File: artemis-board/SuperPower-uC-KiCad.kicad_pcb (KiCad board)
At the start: 4 copper layers, 45.1 x 45.1 mm, 97 parts, among them J1 Battery connector, J10 External NTC, J2 Thermistor, J3 USB_B_Micro, J4 Solar in, J8 regulator board, Q1 2N7002, Q10 AO3401A, Q11 2N7002, Q2 2N7002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

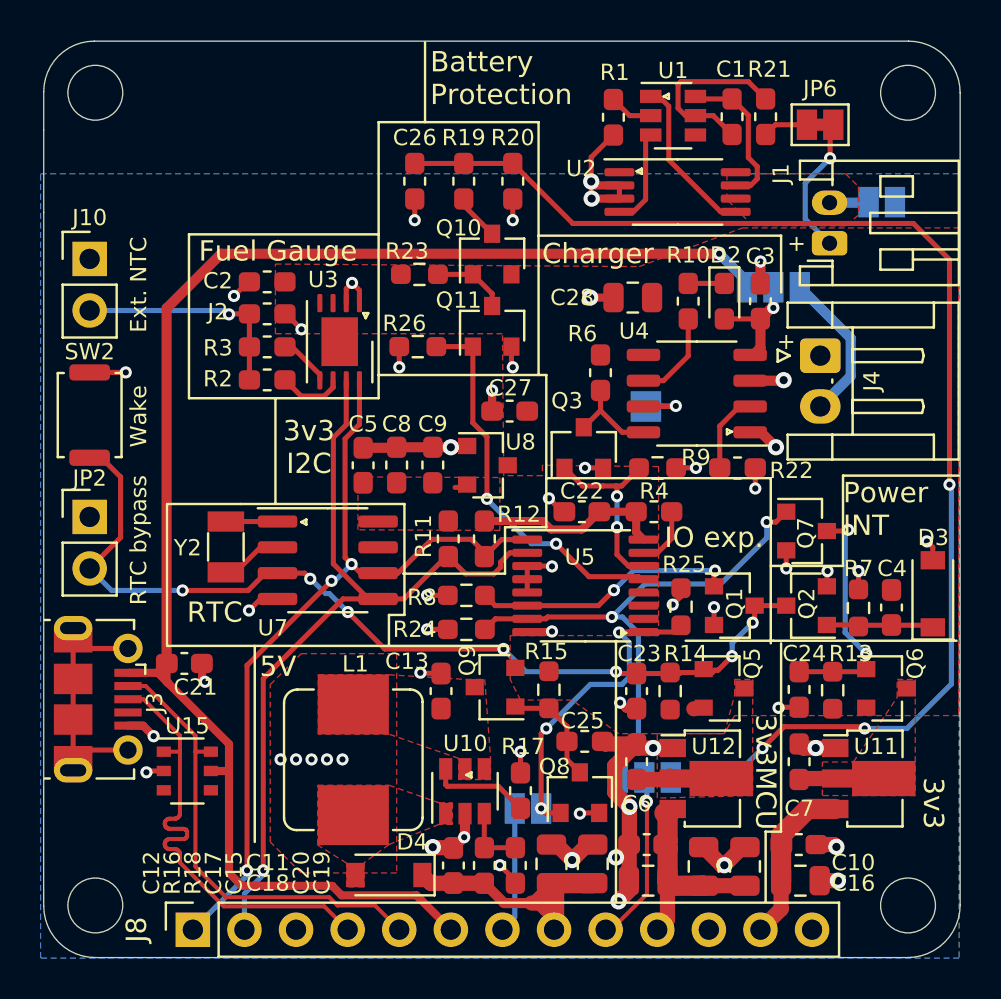
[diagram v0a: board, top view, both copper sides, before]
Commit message: added WLCSP9 footprint for LC709203
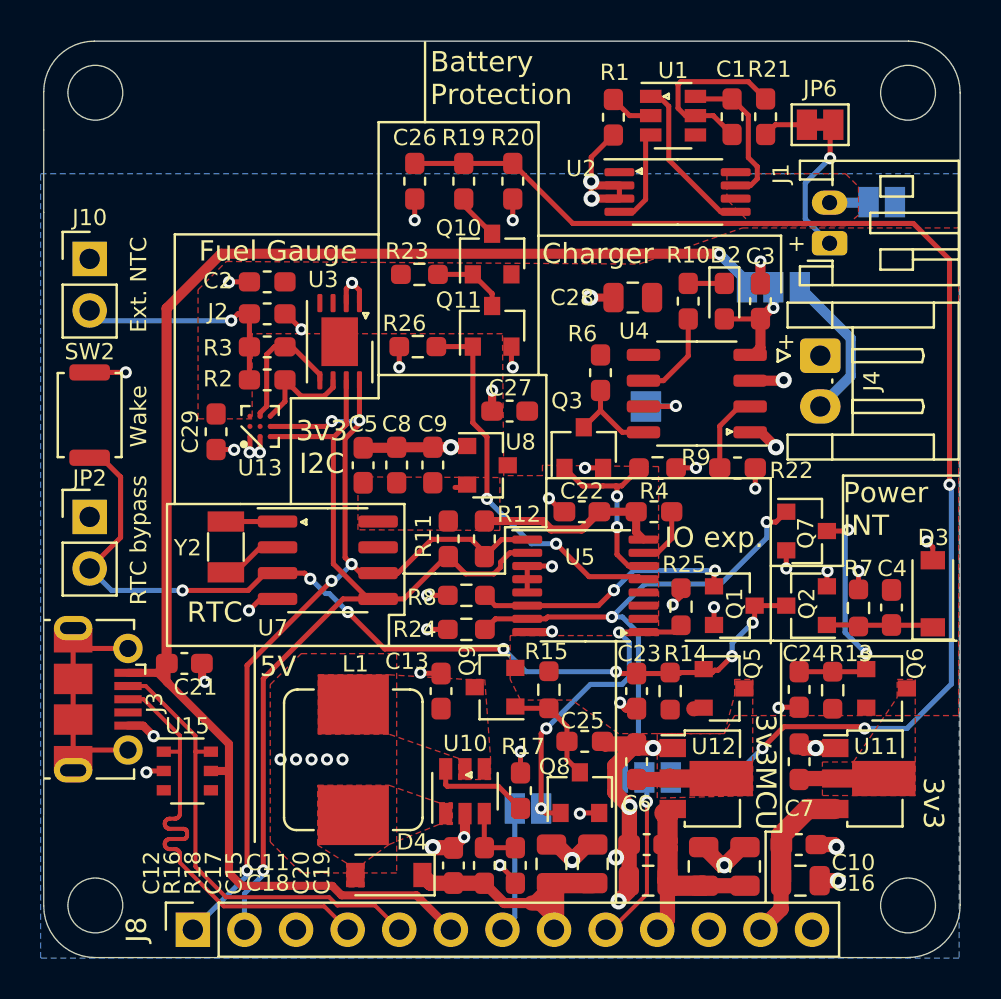
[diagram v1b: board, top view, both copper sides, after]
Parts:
- added C29: 0.1µF, Capacitor_SMD:C_0603_1608Metric_Pad1.05x0.95mm_HandSolder, F.Cu at (141.7, 97.5)
- added U13: LC709203FXE, Package_CSP:WLCSP-9_3x3_1.76x1.6mm, F.Cu at (143.9, 97.3)
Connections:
- net Net-(R2-Pad1) renamed /Charging Module/T1
- net Net-(R3-Pad1) renamed /Charging Module/T2
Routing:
- net /SCL: track 41.9 -> 46.7 mm, vias 3 -> 5
- net /Charging Module/T2: track 2.57 -> 6.80 mm
- net /SDA: track 42.6 -> 45.8 mm
- net GND: track 81.1 -> 83.6 mm, vias 56 -> 59
- net /Charging Module/T1: track 3.22 -> 5.62 mm

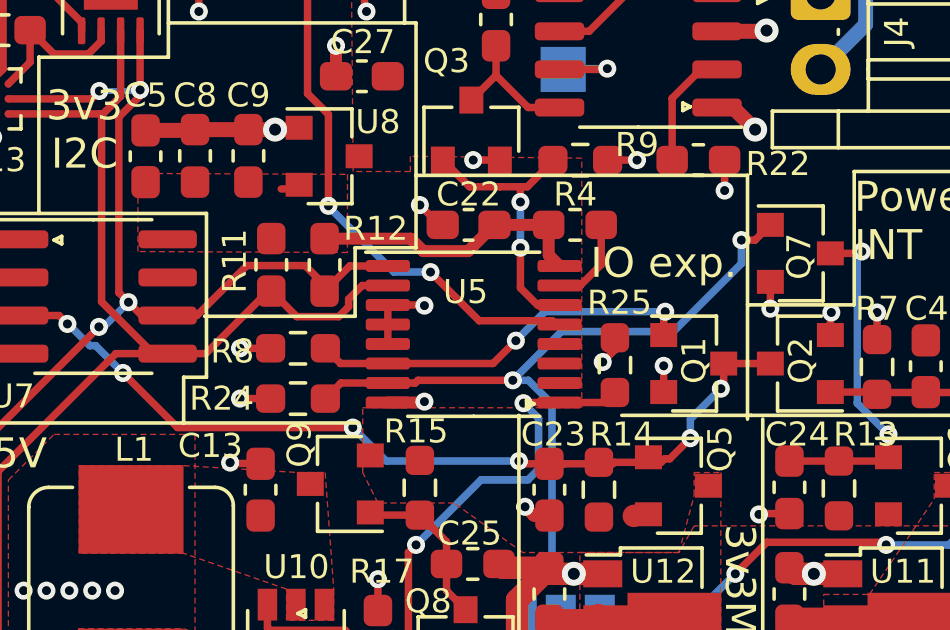
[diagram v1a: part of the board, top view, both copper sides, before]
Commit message: added datasheet for pca9557 and connected ~INT to another pin
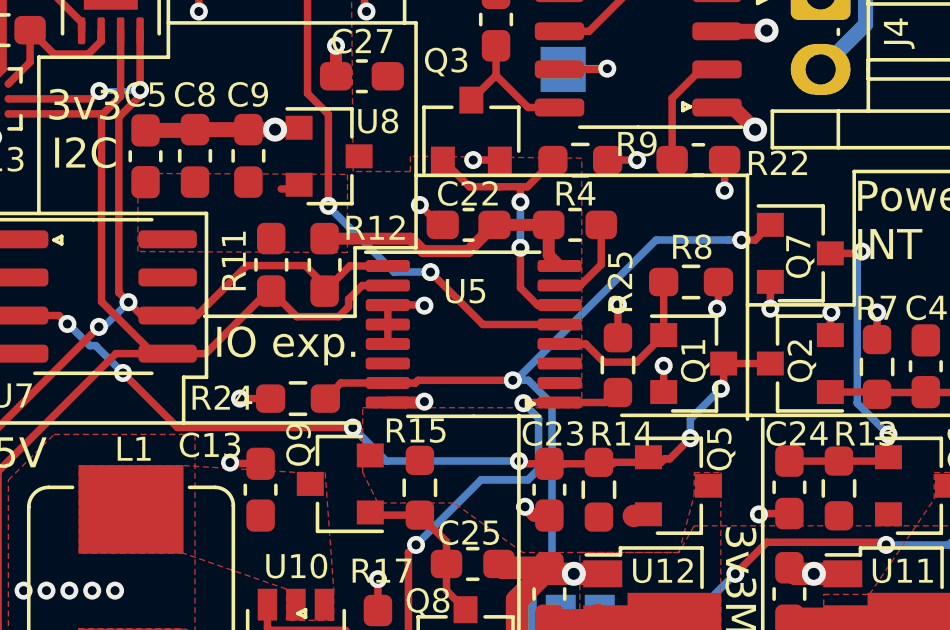
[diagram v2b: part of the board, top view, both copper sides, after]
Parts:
- moved R8 13.3 mm to (167.1, 103.4), turned to 180 degrees
- moved R25 0.10 mm to (164.7, 106.1)
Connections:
- U5 pad 12: Net-(U5-Pad12) -> /RTC and Cut-Off Module/~INT
- U5 pad 6: /RTC and Cut-Off Module/~INT -> Net-(U5-Pad6)
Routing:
- net /RTC and Cut-Off Module/~INT: track 13.1 -> 5.86 mm, vias 2 -> 0

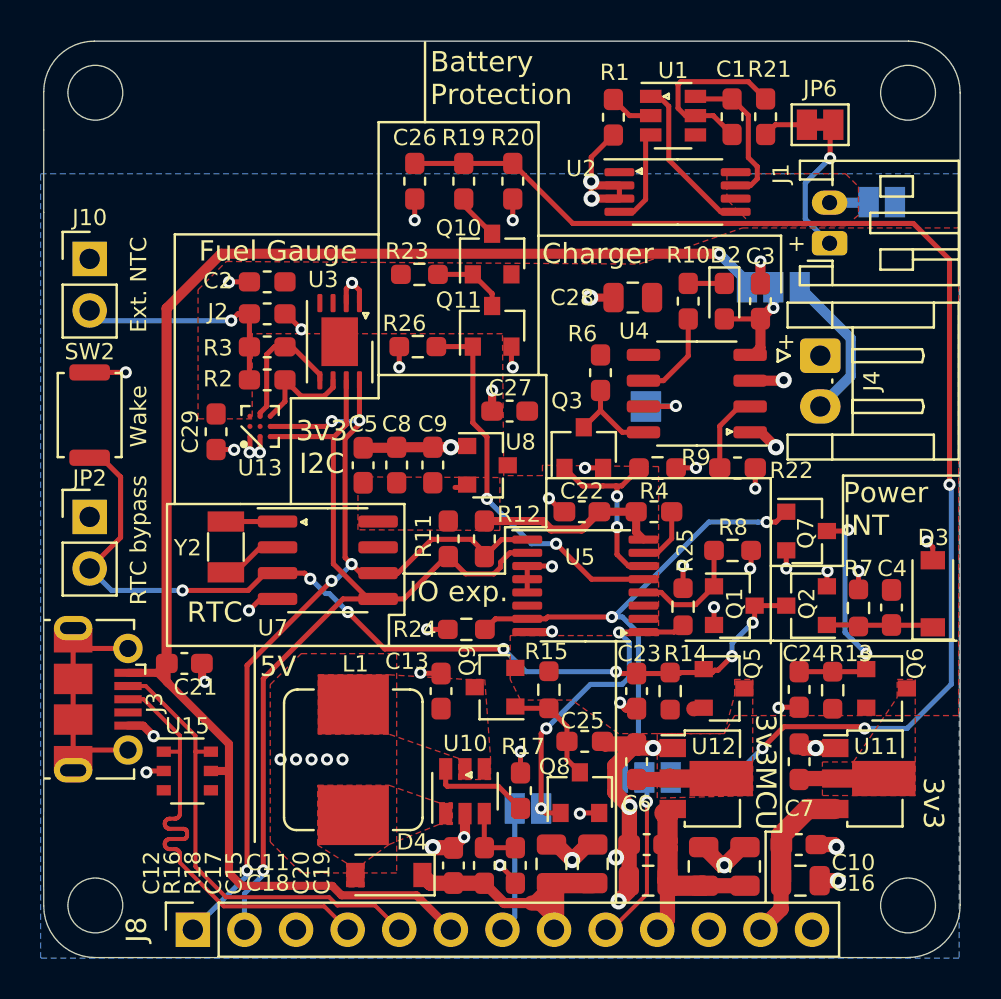
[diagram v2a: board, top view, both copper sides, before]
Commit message: alternative package for PCA9557 and smaller silk
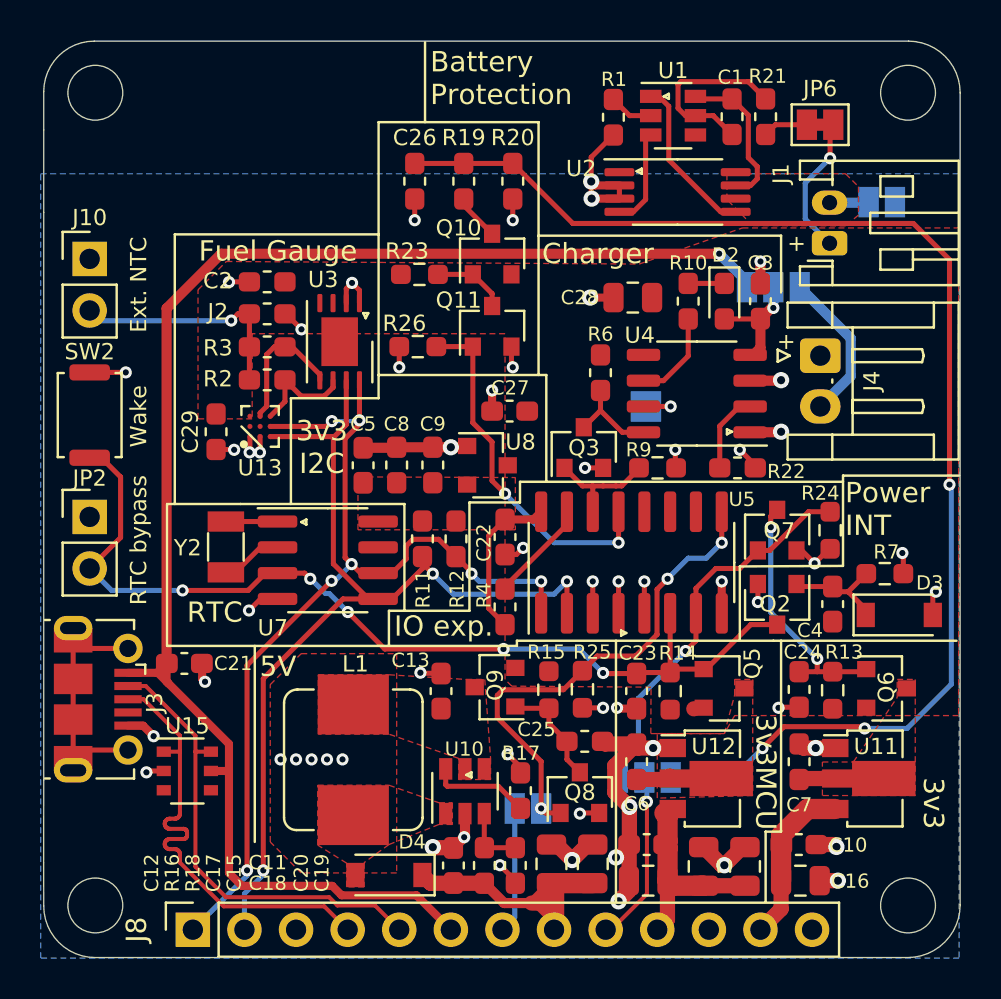
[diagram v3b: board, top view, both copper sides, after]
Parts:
- removed Q1: 2N7002, Package_TO_SOT_SMD:SOT-23
- removed R8: 1M, Resistor_SMD:R_0603_1608Metric_Pad0.98x0.95mm_HandSolder
- U5: footprint Package_SO:TSSOP-16_4.4x5mm_P0.65mm -> Package_SO:SOP-16_3.9x9.9mm_P1.27mm
- moved R24 18.6 mm to (171.9, 102.4), turned to 270 degrees
- moved R4 8.70 mm to (155.9, 106.2), turned to 270 degrees
- moved R25 6.41 mm to (159.7, 110.2), turned to 270 degrees
- moved C22 3.98 mm to (155.9, 102.7), turned to 90 degrees
- moved C4 2.90 mm to (172.1, 106.0), turned to 90 degrees
- moved U5 2.54 mm to (162.2, 104.0), turned to 90 degrees
- moved R7 2.13 mm to (174.6, 104.5), turned to 180 degrees
- moved D3 1.95 mm to (175.3, 106.6), turned to 0 degrees
- moved Q2 1.45 mm to (169.3, 106.0), turned to 270 degrees
- moved Q7 1.45 mm to (169.3, 102.4), turned to 90 degrees
- moved R12 1.40 mm to (153.5, 102.8)
- moved R11 1.27 mm to (151.9, 102.8)
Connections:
- U5 pad 12: /RTC and Cut-Off Module/~INT -> Net-(U5-Pad12)
- U5 pad 6: Net-(U5-Pad6) -> /Charging Module/INT
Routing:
- net /RTC and Cut-Off Module/5V_EN: track 15.8 -> 24.5 mm
- net /RTC and Cut-Off Module/3v3V_EN: track 26.4 -> 19.1 mm, vias 2 -> 1
- net /RTC and Cut-Off Module/~INT: track 5.86 -> 0.00 mm
- net /SDA: track 45.8 -> 49.9 mm, vias 1 -> 3
- net /RTC and Cut-Off Module/~CH_DIS: track 9.38 -> 5.71 mm, vias 2 -> 0
- net /SCL: track 46.7 -> 49.3 mm, vias 5 -> 7
- net /Charging Module/3v3_I2C: track 9.87 -> 7.65 mm
- net Net-(R4-Pad1): track 3.00 -> 5.07 mm
- net /Charging Module/INT: track 46.4 -> 48.0 mm, vias 7 -> 5
- net Net-(Q11-Pad1): track 19.0 -> 17.8 mm
- net GND: track 83.6 -> 84.6 mm, vias 59 -> 58
- net Net-(C24-Pad1): track 11.8 -> 12.4 mm
- net Net-(TP4-Pad1): track 2.93 -> 2.40 mm

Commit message: added reverse polarity protection to power input
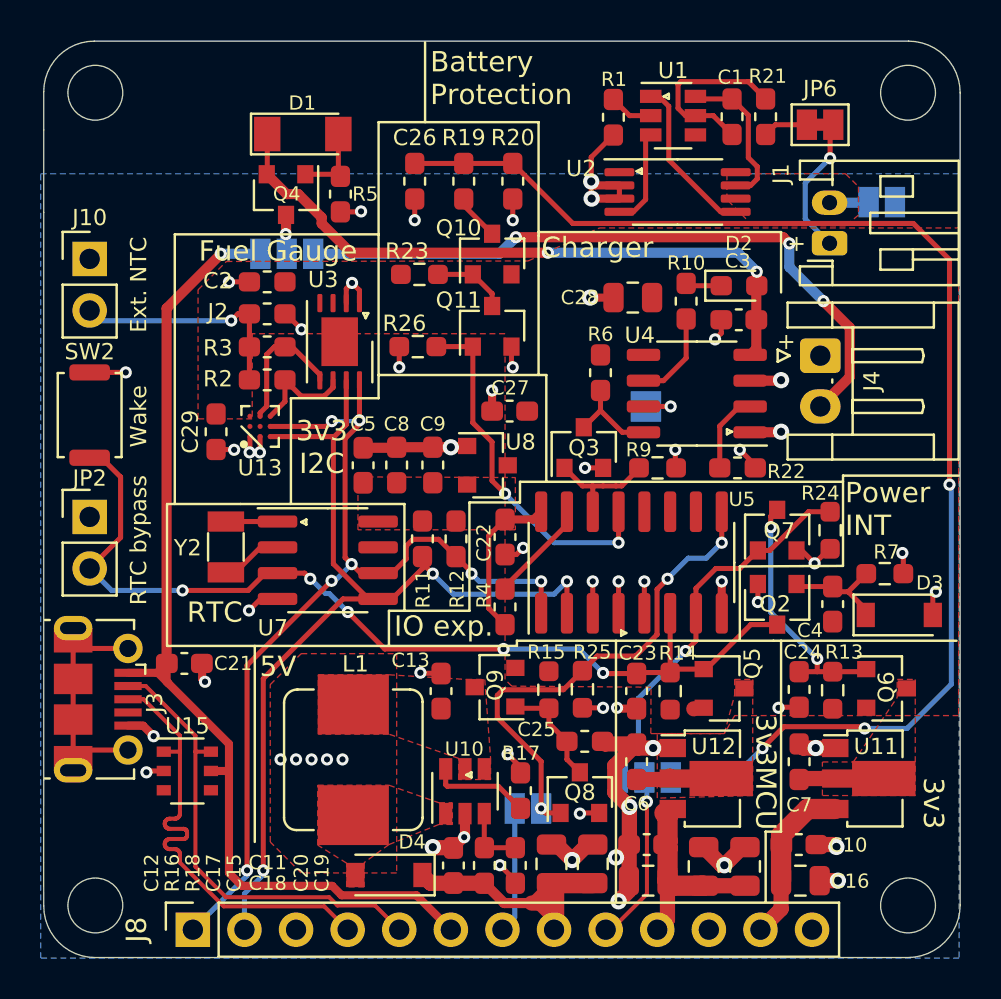
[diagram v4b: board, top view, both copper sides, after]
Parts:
- added D1: ZMM5V6, Diode_SMD:D_MiniMELF, F.Cu at (146.0, 82.9)
- added Q4: AO3401A, Package_TO_SOT_SMD:SOT-23, F.Cu at (145.2, 85.9)
- added R5: 180k, Resistor_SMD:R_0603_1608Metric_Pad1.05x0.95mm_HandSolder, F.Cu at (147.8, 85.8)
- moved JP1 24.0 mm to (145.2, 88.8)
- moved C3 1.41 mm to (167.4, 92.0), turned to 180 degrees
- moved D2 1.05 mm to (167.4, 90.3), turned to 0 degrees
- moved R10 0.10 mm to (164.8, 91.1)
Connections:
- JP1 pad 2: /Charger I/O/VCHARGE -> Net-(JP1-Pad2)
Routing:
- net /Charger I/O/VCHARGE: track 6.69 -> 33.6 mm, vias 1 -> 2
- net Net-(J4-Pad2): track 7.71 -> 33.9 mm, vias 0 -> 3
- net /VBUS: track 75.4 -> 50.7 mm
- net Net-(D1-Pad2): track 0.00 -> 3.75 mm
- net Net-(JP1-Pad2): track 0.00 -> 1.94 mm, vias 0 -> 1
- net GND: track 84.6 -> 85.6 mm, vias 58 -> 59

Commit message: TSSOP version (different pins)
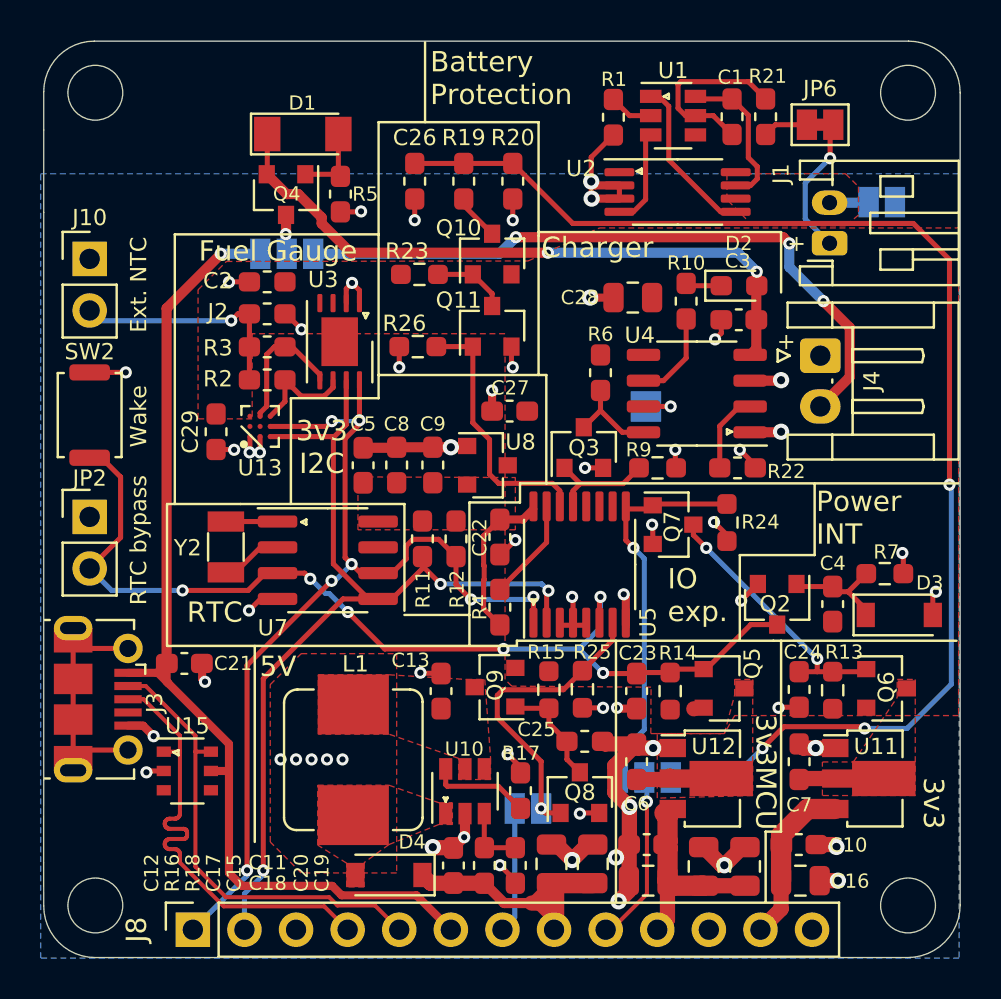
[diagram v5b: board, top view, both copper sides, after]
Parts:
- U5: footprint Package_SO:SOP-16_3.9x9.9mm_P1.27mm -> Package_SO:TSSOP-16_4.4x5mm_P0.65mm
- moved Q7 5.13 mm to (164.2, 102.1), turned to 0 degrees
- moved R24 5.09 mm to (166.9, 102.0)
- moved U5 2.55 mm to (159.6, 104.1)
- moved R4 0.25 mm to (155.7, 106.2)
- moved C22 0.25 mm to (155.7, 102.7)
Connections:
- U5 pad 13: Net-(Q11-Pad1) -> /RTC and Cut-Off Module/~CH_DIS
- U5 pad 14: /RTC and Cut-Off Module/~CH_DIS -> Net-(Q11-Pad1)
- U5 pad 7: /RTC and Cut-Off Module/3v3V_EN -> /RTC and Cut-Off Module/5V_EN
- U5 pad 9: /RTC and Cut-Off Module/5V_EN -> /RTC and Cut-Off Module/3v3V_EN
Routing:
- net /RTC and Cut-Off Module/5V_EN: track 24.5 -> 15.1 mm, vias 3 -> 1
- net Net-(Q11-Pad1): track 17.8 -> 13.0 mm, vias 2 -> 0
- net GND: track 85.6 -> 83.7 mm, vias 59 -> 58
- net /Charging Module/INT: track 48.0 -> 49.6 mm, vias 5 -> 6
- net Net-(C24-Pad1): track 12.4 -> 13.1 mm
- net /SDA: track 49.9 -> 49.3 mm
- net /SCL: track 49.3 -> 49.9 mm
